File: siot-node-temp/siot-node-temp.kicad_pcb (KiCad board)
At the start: 2 copper layers, 21.6 x 21.6 mm, 9 parts, among them J1 Conn_01x03, J2 Conn_01x03, J3 Conn_01x03, J4 Conn_01x03, U1 L78L05_SO8

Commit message: fix hole sizes
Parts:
- J1, J4: footprint Connector_PinHeader_1.27mm:PinHeader_1x03_P1.27mm_Vertical -> bec:xConnect
- J2, J3: footprint Connector_PinHeader_1.27mm:PinHeader_1x03_P1.27mm_Vertical -> Connector_PinHeader_2.54mm:PinHeader_1x03_P2.54mm_Vertical
- moved J1 3.17 mm to (-459.7, -617.9)
- moved J4 3.17 mm to (-443.2, -617.9)
- moved J2 1.91 mm to (-459.1, -631.2)
- moved J3 0.97 mm to (-448.9, -631.2)
- moved C1 0.63 mm to (-446.4, -624.1)
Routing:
- net +5V: track 21.3 -> 23.2 mm
- net +24V: track 29.7 -> 31.1 mm
- net GND: track 14.3 -> 13.6 mm
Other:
- net class Power: trace_width 50 -> 50.000002

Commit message: design updates
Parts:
- C1, C2: value 0.1uF -> 2.2uF
- J1, J4: value Conn_01x03 -> xConnect_smd; footprint bec:xConnect -> BEC:xConnect_smd
- J2, J3: footprint Connector_PinHeader_2.54mm:PinHeader_1x03_P2.54mm_Vertical -> BEC:1x03_solder-pads
- U1: value L78L05_SO8 -> ADP7142AUJZ-3.3; footprint Package_SO:SOIC-8_3.9x4.9mm_P1.27mm -> Package_TO_SOT_SMD:TSOT-23-5
- moved R2 887.7 mm to (113.8, 60.4)
- moved J3 883.7 mm to (105.9, 56.6)
- moved J2 883.2 mm to (95.0, 56.6)
- moved R1 881.6 mm to (94.6, 60.7)
- moved J1 880.9 mm to (101.7, 60.9), turned to 0 degrees
- moved C2 880.8 mm to (94.8, 63.4), turned to 0 degrees
- moved C1 880.0 mm to (94.8, 69.8), turned to 0 degrees
- moved U1 878.9 mm to (94.9, 66.6), turned to 90 degrees
- moved J4 873.5 mm to (106.7, 60.9), turned to 0 degrees
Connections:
- C2 pad 1: +5V -> +3V3
- J2 pad 1: +5V -> +3V3
- J3 pad 1: +5V -> +3V3
- U1 pad 1: +5V -> +24V
- U1 pad 3: GND -> Net-(U1-Pad3)
- U1 pad 4: Net-(U1-Pad4) -> +3V3
- U1 pad 5: Net-(U1-Pad5) -> +3V3
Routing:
- net +3V3: track 0.00 -> 25.3 mm
- net +5V: track 23.2 -> 0.00 mm
- net +24V: track 31.1 -> 18.0 mm
- net GND: track 13.6 -> 4.40 mm, vias 4 -> 12
- net /data: track 33.6 -> 25.1 mm, vias 0 -> 2
- net Net-(J3-Pad2): track 2.92 -> 5.65 mm
- net Net-(J2-Pad2): track 2.80 -> 5.27 mm

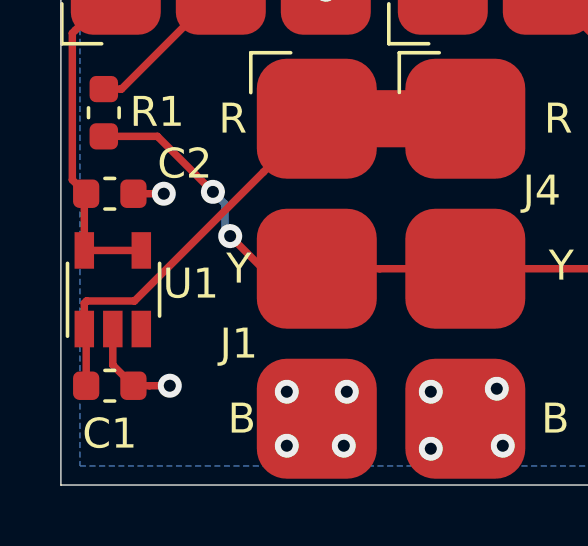
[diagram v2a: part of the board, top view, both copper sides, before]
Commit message: fix missing en on temp board
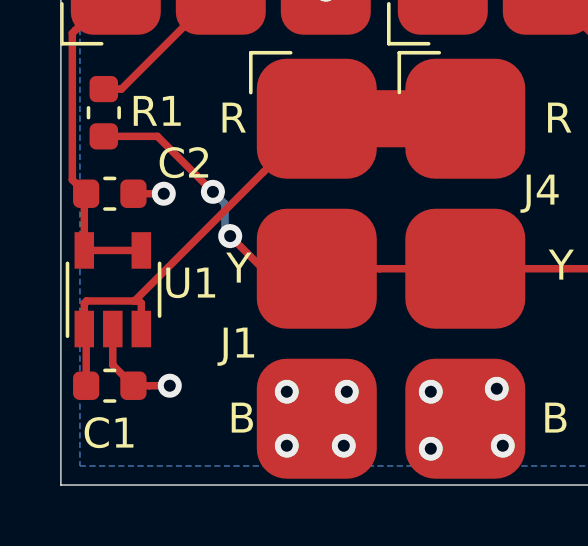
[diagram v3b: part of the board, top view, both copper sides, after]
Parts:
- C1, C2: value 2.2uF -> 2.2uF_50V
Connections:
- U1 pad 3: Net-(U1-Pad3) -> +24V
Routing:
- net +24V: track 18.0 -> 19.1 mm

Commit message: updates
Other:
- board text added: "B"
- board text added: "R"
- board text added: "Y"
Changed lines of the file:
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@@
   (general
     (thickness 1.6)
-    (drawings 4)
+    (drawings 10)
     (tracks 58)
     (zones 0)
@@
     (tags "Through hole 1x03 single row")
     (attr smd)
-    (fp_text reference J3 (at 2.3 3.3 180) (layer F.SilkS)
+    (fp_text reference J3 (at -2.4 3.7 180) (layer F.SilkS)
       (effects (font (size 1 1) (thickness 0.15)))
     )
@@
     (tags "Through hole 1x03 single row")
     (attr smd)
-    (fp_text reference J2 (at 2.3 3.5 180) (layer F.SilkS)
+    (fp_text reference J2 (at -2.4 3.2 180) (layer F.SilkS)
       (effects (font (size 1 1) (thickness 0.15)))
     )
@@
     )
   )
+  (gr_text B (at 112.8 54.2) (layer F.SilkS)
+    (effects (font (size 1 1) (thickness 0.15)))
+  )
+  (gr_text Y (at 109.4 54.2) (layer F.SilkS)
+    (effects (font (size 1 1) (thickness 0.15)))
+  )
+  (gr_text R (at 105.8 54.2) (layer F.SilkS)
+    (effects (font (size 1 1) (thickness 0.15)))
+  )
+  (gr_text B (at 102 54.2) (layer F.SilkS)
+    (effects (font (size 1 1) (thickness 0.15)))
+  )
+  (gr_text Y (at 98.6 54.2) (layer F.SilkS)
+    (effects (font (size 1 1) (thickness 0.15)))
+  )
+  (gr_text R (at 95 54.2) (layer F.SilkS)
+    (effects (font (size 1 1) (thickness 0.15)))
+  )
   (gr_line (start 93.17 51.52) (end 93.17 73.11) (layer Edge.Cuts) (width 0.05))

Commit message: updates
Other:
- board text added: "SIOT Temp v2"
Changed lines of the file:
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@@
   (general
     (thickness 1.6)
-    (drawings 10)
+    (drawings 11)
     (tracks 58)
     (zones 0)
@@
     )
   )
+  (gr_text "SIOT Temp\nv2" (at 112.4 67.8 90) (layer F.SilkS)
+    (effects (font (size 1 1) (thickness 0.2)))
+  )
   (gr_text B (at 112.8 54.2) (layer F.SilkS)
